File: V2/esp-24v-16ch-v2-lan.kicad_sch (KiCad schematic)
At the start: 28 parts, among them J7 ETHERNET, U5 LAN8710A

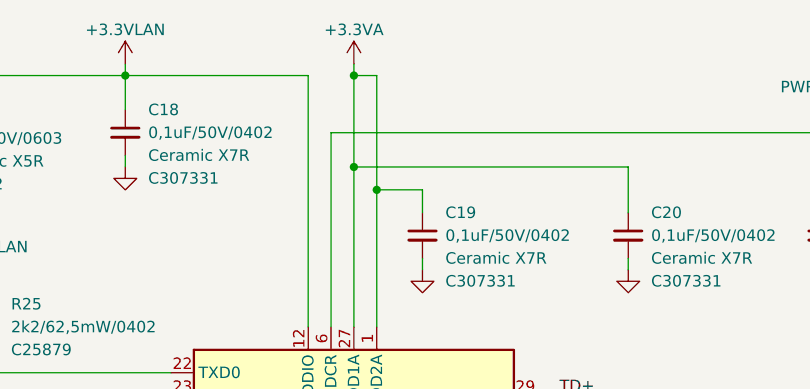
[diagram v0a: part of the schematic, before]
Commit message: Adjusted footprint
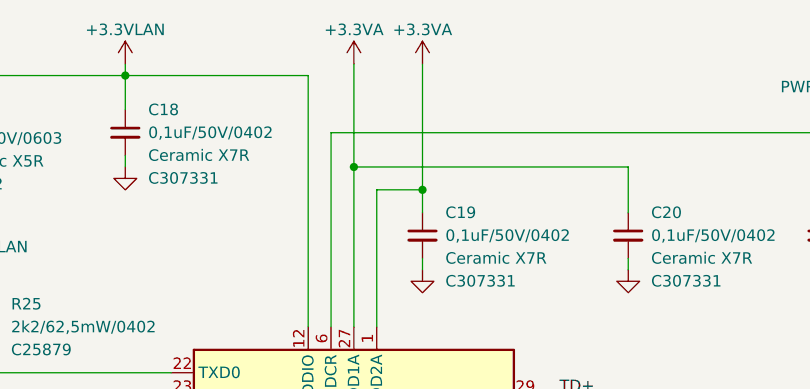
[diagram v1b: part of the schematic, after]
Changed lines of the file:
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@@
   (junction (at 110.49 73.66) (diameter 0) (color 0 0 0 0)
   )
-  (junction (at 179.07 38.1) (diameter 0) (color 0 0 0 0)
-  )
   (junction (at 151.13 25.4) (diameter 0) (color 0 0 0 0)
   )
@@
   (junction (at 153.67 63.5) (diameter 0) (color 0 0 0 0)
   )
-  (junction (at 176.53 25.4) (diameter 0) (color 0 0 0 0)
-  )
   (junction (at 135.89 71.12) (diameter 0) (color 0 0 0 0)
   )
@@
   )
   (junction (at 237.49 77.47) (diameter 0) (color 0 0 0 0)
+  )
+  (junction (at 184.15 38.1) (diameter 0) (color 0 0 0 0)
   )
   (junction (at 228.6 31.75) (diameter 0) (color 0 0 0 0)
@@
     (stroke (width 0) (type default))
   )
-  (wire (pts (xy 176.53 25.4) (xy 176.53 35.56))
+  (wire (pts (xy 176.53 24.13) (xy 176.53 35.56))
     (stroke (width 0) (type default))
   )
@@
     (stroke (width 0) (type default))
   )
-  (wire (pts (xy 176.53 24.13) (xy 176.53 25.4))
-    (stroke (width 0) (type default))
-  )
   (wire (pts (xy 229.87 125.73) (xy 248.92 125.73))
     (stroke (width 0) (type default))
@@
     (stroke (width 0) (type default))
   )
-  (wire (pts (xy 176.53 25.4) (xy 179.07 25.4))
-    (stroke (width 0) (type default))
-  )
   (wire (pts (xy 151.13 25.4) (xy 171.45 25.4))
     (stroke (width 0) (type default))
@@
     (stroke (width 0) (type default))
   )
-  (wire (pts (xy 179.07 25.4) (xy 179.07 38.1))
-    (stroke (width 0) (type default))
-  )
   (wire (pts (xy 256.54 138.43) (xy 266.7 138.43))
     (stroke (width 0) (type default))
@@
   )
   (wire (pts (xy 38.1 81.28) (xy 156.21 81.28))
+    (stroke (width 0) (type default))
+  )
+  (wire (pts (xy 184.15 24.13) (xy 184.15 38.1))
     (stroke (width 0) (type default))
   )
@@
         )
       )
+    )
+  )
+  (symbol (lib_id "power:+3.3VA") (at 184.15 24.13 0) (unit 1)
+    (in_bom yes) (on_board yes) (dnp no)
+    (property "Reference" "#PWR0191" (at 184.15 27.94 0)
+      (effects (font (size 1.27 1.27)) hide)
+    )
+    (property "Value" "+3.3VA" (at 184.15 20.32 0)
+      (effects (font (size 1.27 1.27)))
+    )
+    (property "Footprint" "" (at 184.15 24.13 0)
+      (effects (font (size 1.27 1.27)) hide)
+    )
+    (property "Datasheet" "" (at 184.15 24.13 0)
+      (effects (font (size 1.27 1.27)) hide)
+    )
+    (pin "1")
+    (instances
+      (project "esp-24v-16ch-v2"
+        (path "/2bc5a21a-1d79-419d-a592-6852cc07b00a/c76fc600-a423-4f14-bc69-e86c7c986b21"
+          (reference "#PWR0191") (unit 1)
+        )
+      )
+      (project "ESP-24v-16ch-V2-lan"
+        (path "/6c33f4ff-7ffb-4387-9626-ca1bbece1989"
+          (reference "#PWR055") (unit 1)
+        )
+      )
